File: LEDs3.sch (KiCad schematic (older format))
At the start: 60 parts

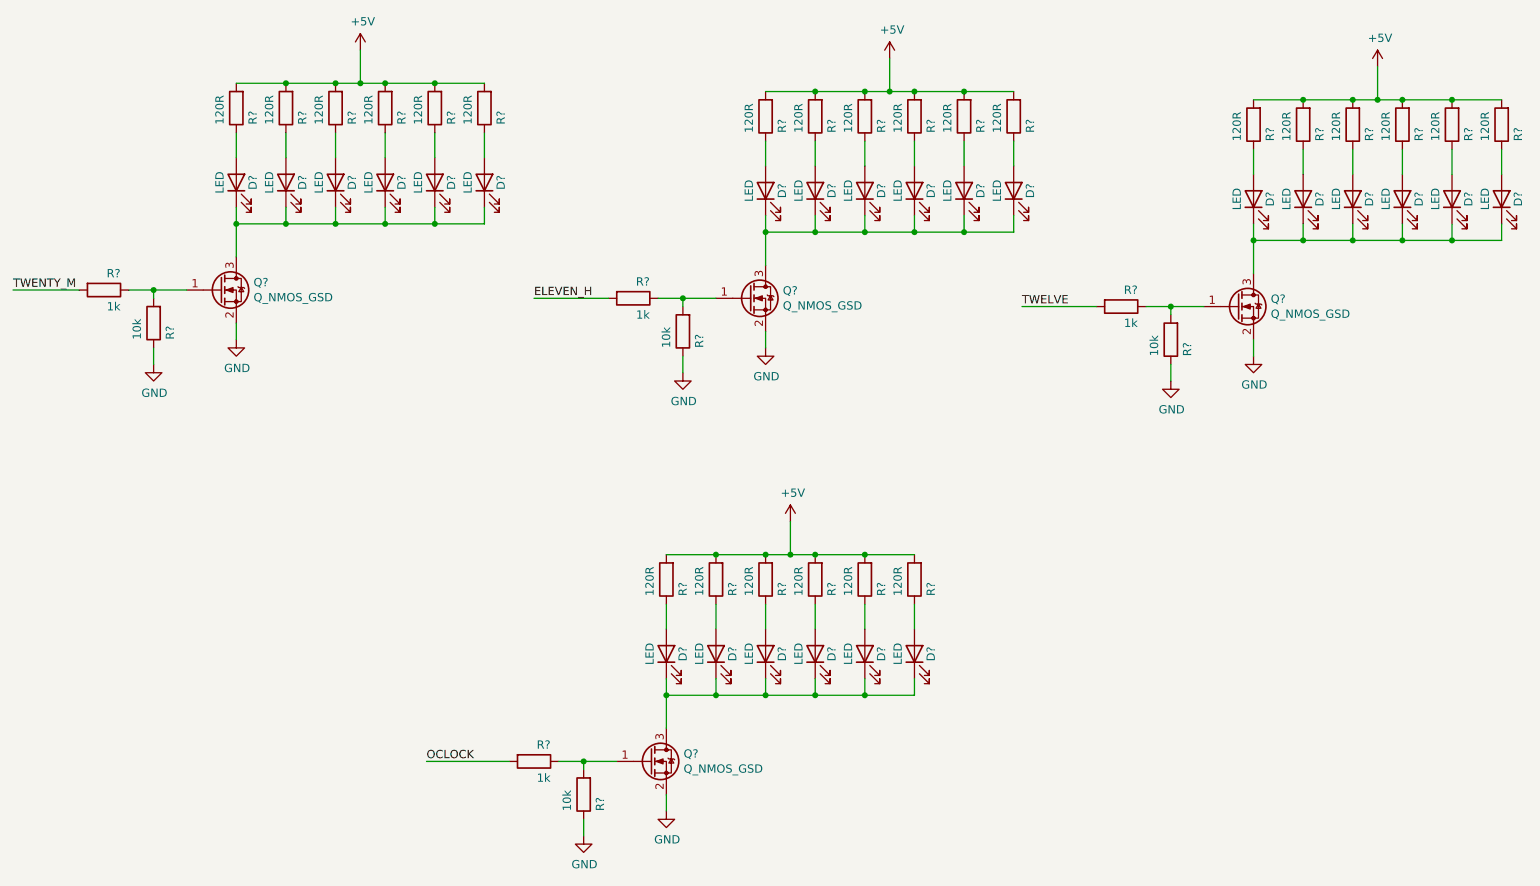
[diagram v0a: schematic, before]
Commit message: Schematic is almost finished. The MCLR circuit needs completing, the hour/minute inputs also need their input protection.
After that, I might have one of the guys from work review it. But, who knows.
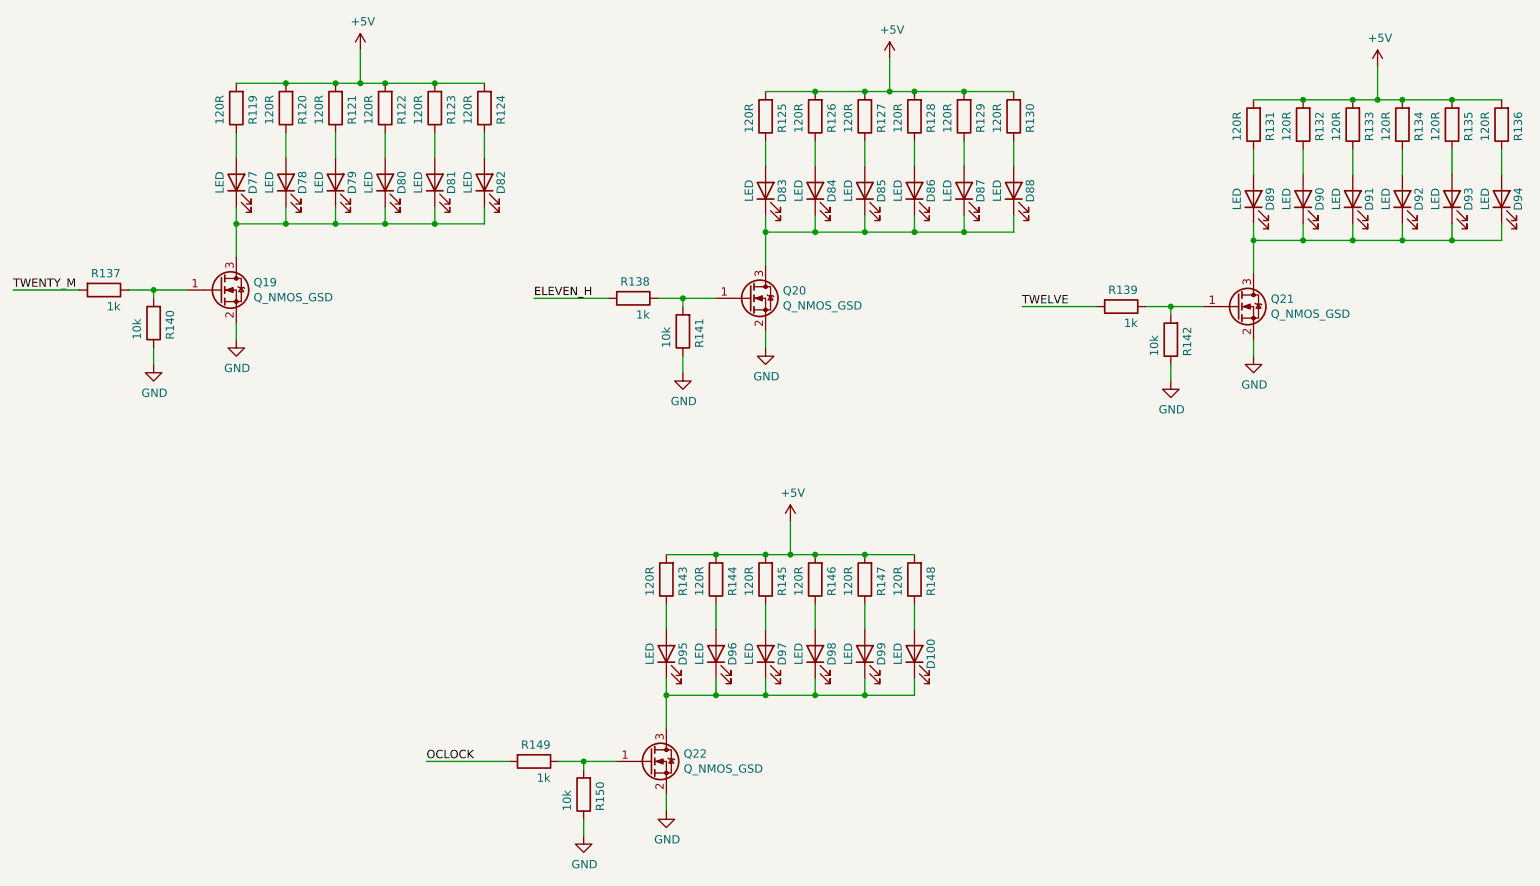
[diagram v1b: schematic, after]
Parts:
- gave numbers to parts that had none: 60
